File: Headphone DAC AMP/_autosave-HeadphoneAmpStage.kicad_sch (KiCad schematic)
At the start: 66 parts, among them U3 TPA6120A2DWP, U4 OPA1612AxD, U5 OPA1612AxD

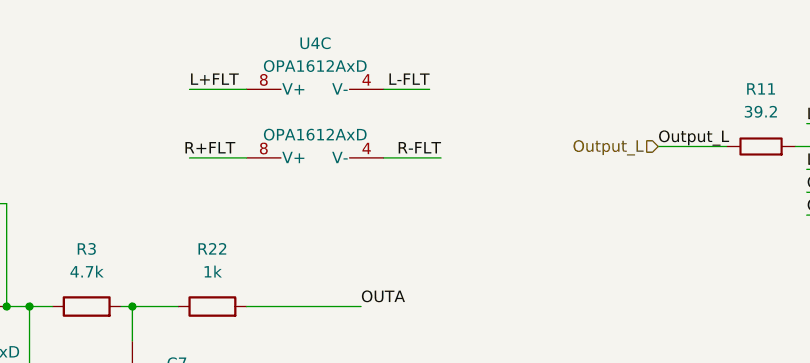
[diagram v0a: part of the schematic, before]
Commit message: Added PCB Filtering
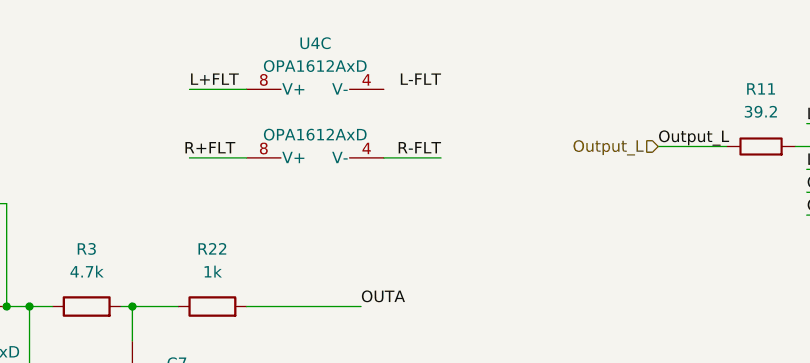
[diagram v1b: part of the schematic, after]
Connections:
- net +5V: no longer U4.4 (V-)
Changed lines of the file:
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@@
-	(wire
-		(pts
-			(xy 115.57 22.86) (xy 120.65 22.86)
-		)
-		(stroke
-			(width 0)
-			(type default)
-		)
-	)
 	(wire
 		(pts
@@
 	)
 	(label "L-FLT"
-		(at 120.65 22.86 180)
+		(at 121.92 22.86 180)
 		(effects
 			(font
